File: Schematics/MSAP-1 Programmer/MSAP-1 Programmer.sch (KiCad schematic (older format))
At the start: 7 parts, among them M1 SD_Card, M2 SSD1306, SW1 SW_Push, U1 74HC595, U2 74HC595

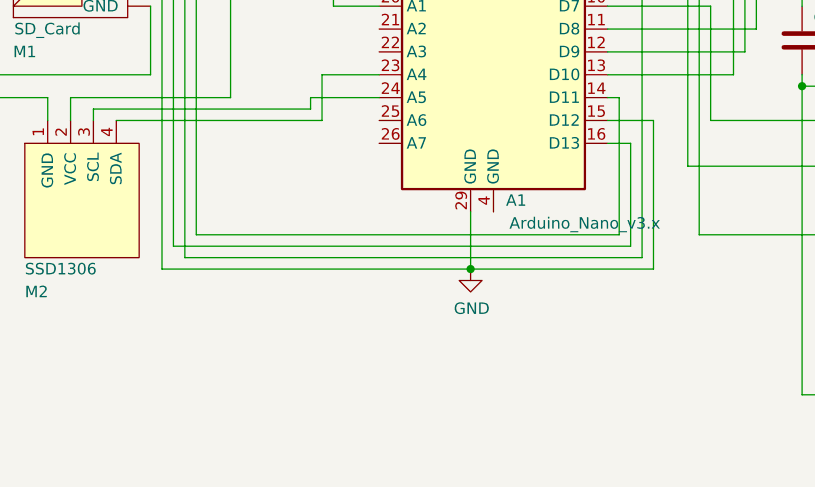
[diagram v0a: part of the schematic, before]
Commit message: fixed the GND link in Nano
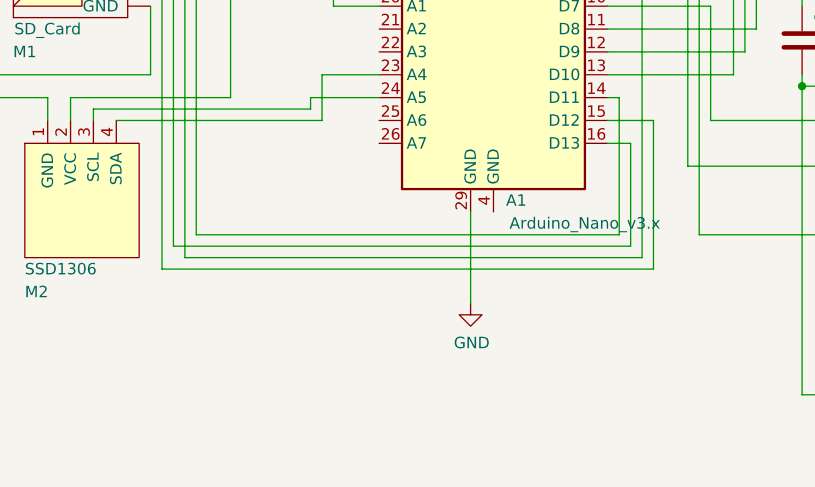
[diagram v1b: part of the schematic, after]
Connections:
- net GND: no longer A1.15 (D12)
- new net: A1.15 (D12), M1.~ (VCC)

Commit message: Added OE wire to GND for U1 and U2
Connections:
- net GND: now also U1.13 (~OE), U2.13 (~OE)
- no-connect marks 0 -> 13
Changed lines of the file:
@@
 Connection ~ 7250 5350
 Wire Wire Line
-	7250 5350 6750 5350
+	7250 5350 6850 5350
 Wire Wire Line
 	6750 4000 6750 5350
@@
 Wire Wire Line
 	5300 4550 5300 4950
+Wire Wire Line
+	6850 4750 6850 5350
+Connection ~ 6850 5350
+Wire Wire Line
+	6850 5350 6750 5350
+Wire Wire Line
+	6850 3100 6600 3100
+Wire Wire Line
+	6600 3100 6600 4000
+Wire Wire Line
+	6600 4000 6750 4000
+NoConn ~ 7650 5050
+NoConn ~ 7650 3400
+NoConn ~ 5900 3150
+NoConn ~ 5900 3050
+NoConn ~ 5900 2950
+NoConn ~ 4900 4250
+NoConn ~ 4900 4150
+NoConn ~ 5400 4550
+NoConn ~ 4900 3350
+NoConn ~ 4900 3050
+NoConn ~ 4900 2950
+NoConn ~ 5300 2550
+NoConn ~ 5500 2550
 Wire Bus Line
 	8100 4100 8100 5050

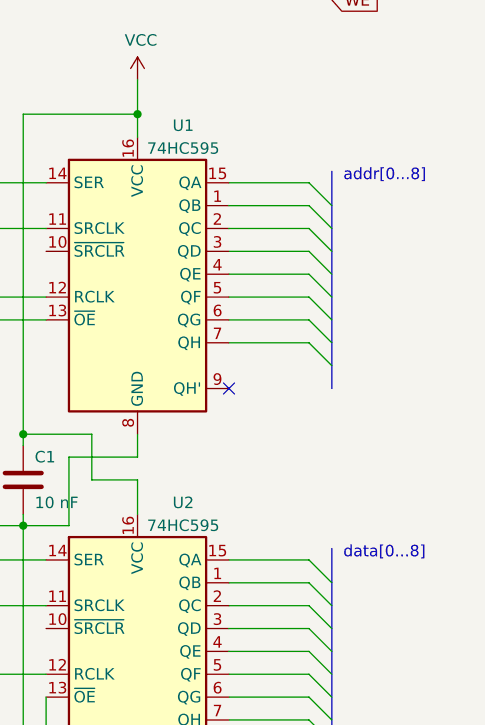
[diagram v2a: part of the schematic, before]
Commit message: corrected the bus length
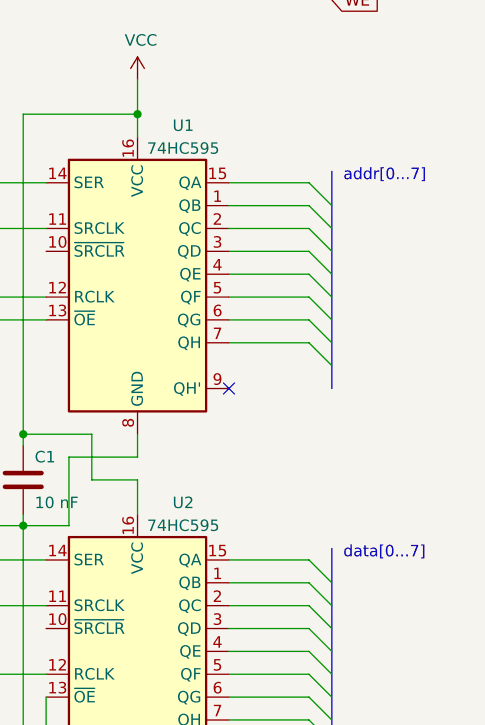
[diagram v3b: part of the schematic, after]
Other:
- note added: "addr[0...7]"
- note added: "data[0...7]"
- note removed: "addr[0...8]"
- note removed: "data[0...8]"
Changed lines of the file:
@@
 	8000 4850 8100 4950
 Text Notes 8150 2500 0    50   ~ 0
-addr[0...8]
+addr[0...7]
 Text Notes 8150 4150 0    50   ~ 0
-data[0...8]
+data[0...7]
 $Comp
 L 74xx:74HC595 U1
